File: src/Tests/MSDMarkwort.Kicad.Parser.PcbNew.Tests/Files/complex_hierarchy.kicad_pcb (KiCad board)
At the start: 2 copper layers, 100.7 x 80 mm, 68 parts, among them P101 CONN_2, P102 CONN_2, P201 CONN_2, P202 CONN_2, P301 CONN_2, P302 CONN_2, Q201 MPSA92, Q202 MPSA42, Q203 MPSA92, Q204 MPSA42, Q301 MPSA92, Q302 MPSA42, Q303 MPSA92, Q304 MPSA42, U101 78L05, U102 ICL7660, U201 LM358N, U301 LM358N

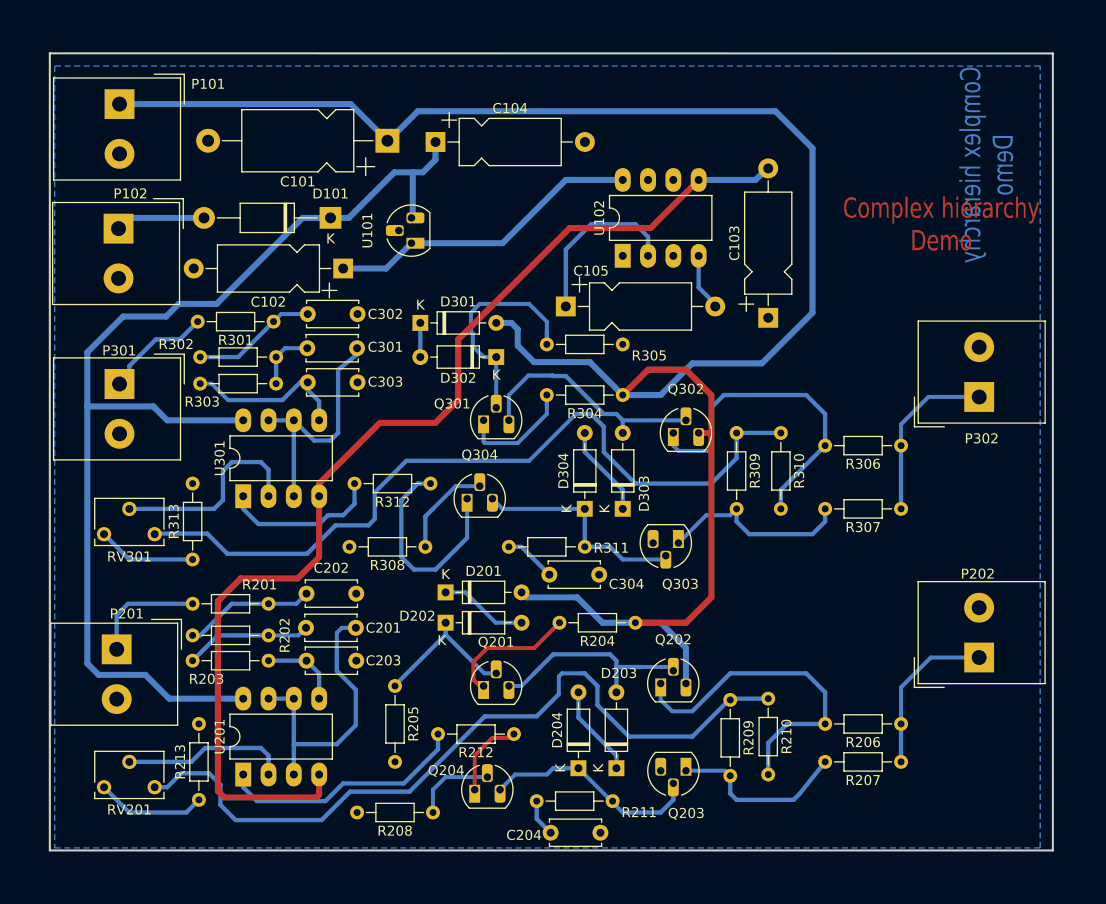
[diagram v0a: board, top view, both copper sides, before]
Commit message: eeschema parser added (#2)
* s-expression parser added
* eeschema parser  & models added
* readme changed
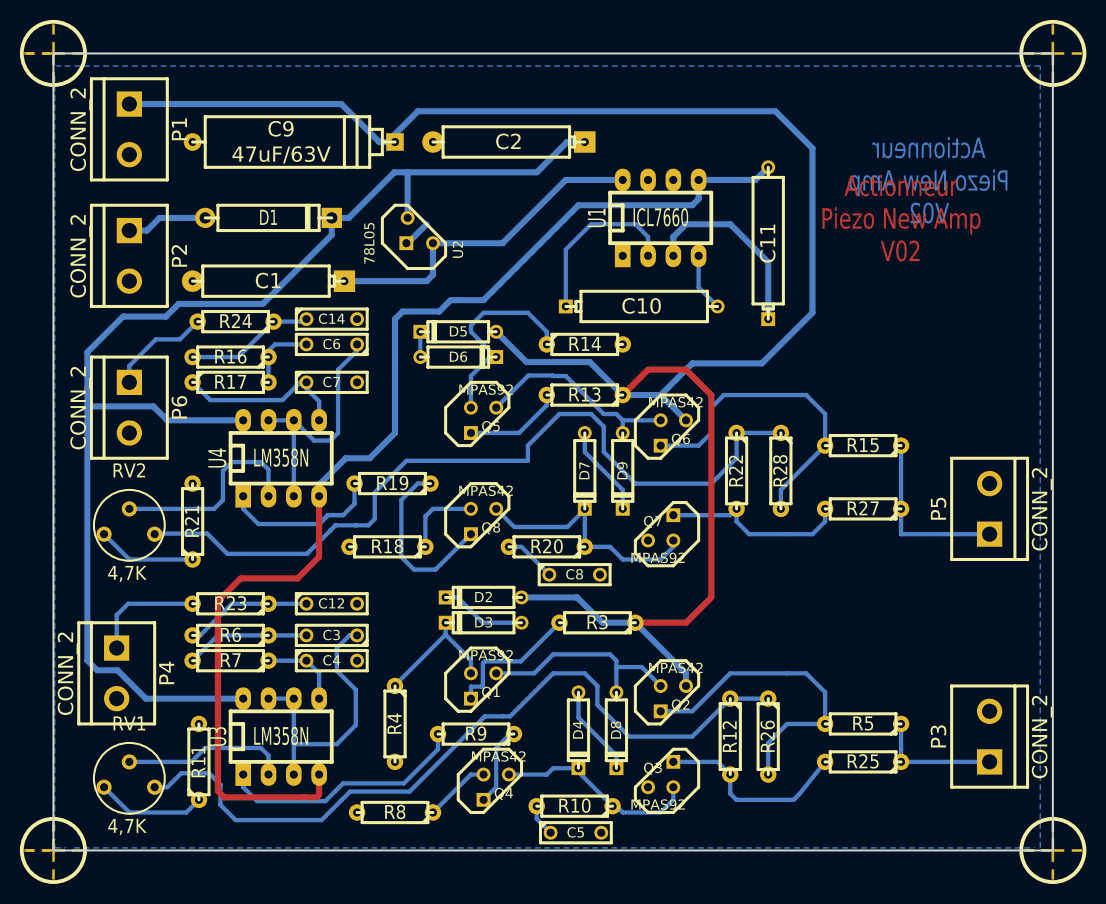
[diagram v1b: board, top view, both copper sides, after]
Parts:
- removed C101: 47uF/63V, Capacitor_THT:CP_Axial_L11.0mm_D6.0mm_P18.00mm_Horizontal
- removed C102: 47uF, Capacitor_THT:CP_Axial_L10.0mm_D4.5mm_P15.00mm_Horizontal
- removed C103, C105: 10uF, Capacitor_THT:CP_Axial_L10.0mm_D4.5mm_P15.00mm_Horizontal
- removed C104: 47uF/20V, Capacitor_THT:CP_Axial_L10.0mm_D4.5mm_P15.00mm_Horizontal
- removed C201, C301: 15nF, Capacitor_THT:C_Disc_D5.0mm_W2.5mm_P5.00mm
- removed C202, C302: 150nF, Capacitor_THT:C_Disc_D5.0mm_W2.5mm_P5.00mm
- removed C203, C303: 4.7nF, Capacitor_THT:C_Disc_D5.0mm_W2.5mm_P5.00mm
- removed C204, C304: 820pF, Capacitor_THT:C_Disc_D5.0mm_W2.5mm_P5.00mm
- removed D101: 1N4007, Diode_THT:D_DO-41_SOD81_P12.70mm_Horizontal
- removed D201, D202, D203, D204, D301, D302, D303, D304: 1N4148, Diode_THT:D_DO-35_SOD27_P7.62mm_Horizontal
- removed P101, P102, P201, P202, P301, P302: CONN_2, TerminalBlock_Altech:Altech_AK300_1x02_P5.00mm_45-Degree
- removed Q201, Q203, Q301, Q303: MPSA92, Package_TO_SOT_THT:TO-92_HandSolder
- removed Q202, Q204, Q302, Q304: MPSA42, Package_TO_SOT_THT:TO-92_HandSolder
- removed R201, R208, R212, R301, R308, R312: 1K, Resistor_THT:R_Axial_DIN0204_L3.6mm_D1.6mm_P7.62mm_Horizontal
- removed R202, R203, R302, R303: 22K, Resistor_THT:R_Axial_DIN0204_L3.6mm_D1.6mm_P7.62mm_Horizontal
- removed R204, R304: 470, Resistor_THT:R_Axial_DIN0204_L3.6mm_D1.6mm_P7.62mm_Horizontal
- removed R205, R209, R210, R305, R309, R310: 220K, Resistor_THT:R_Axial_DIN0204_L3.6mm_D1.6mm_P7.62mm_Horizontal
- removed R206, R207, R306, R307: 47, Resistor_THT:R_Axial_DIN0204_L3.6mm_D1.6mm_P7.62mm_Horizontal
- removed R211, R311: 5,6K, Resistor_THT:R_Axial_DIN0204_L3.6mm_D1.6mm_P7.62mm_Horizontal
- removed R213, R313: 4,7K, Resistor_THT:R_Axial_DIN0204_L3.6mm_D1.6mm_P7.62mm_Horizontal
- removed RV201, RV301: 4,7K, Potentiometer_THT:Potentiometer_Bourns_3266W_Vertical
- removed U101: 78L05, Package_TO_SOT_THT:TO-92_HandSolder
- removed U102: ICL7660, Package_DIP:DIP-8_W7.62mm_LongPads
- removed U201, U301: LM358N, Package_DIP:DIP-8_W7.62mm_LongPads
- added C1: 47uF, CP6, F.Cu at (109.9, 74.7)
- added C10: 10uF, CP6, F.Cu at (147.3, 77.2)
- added C11: 10uF, CP6, F.Cu at (160.0, 70.9)
- added C12: 150nF, C2, F.Cu at (116.2, 107.1)
- added C14: 150nF, C2, F.Cu at (116.2, 78.5)
- added C2: 47uF/20V, CP6, F.Cu at (134.0, 60.7)
- added C3: 15nF, C2, F.Cu at (116.2, 110.2)
- added C4: 4,7nF, C2, F.Cu at (116.2, 112.8)
- added C5: 820pF, C2, F.Cu at (140.7, 130.0)
- added C6: 15nF, C2, F.Cu at (116.2, 81.0)
- added C7: 4,7nF, C2, F.Cu at (116.2, 84.8)
- added C8: 820pF, C2, F.Cu at (140.6, 104.1)
- added C9: 47uF/63V, CP8, F.Cu at (112.4, 60.7)
- added D1: 1N4007, D5, F.Cu at (109.9, 68.3)
- added D2: 1N4148, D3, F.Cu at (131.4, 106.4)
- added D3: 1N4148, D3, F.Cu at (131.4, 109.0)
- added D4: 1N4148, D3, F.Cu at (141.0, 119.8)
- added D5: 1N4148, D3, F.Cu at (128.9, 79.8)
- added D6: 1N4148, D3, F.Cu at (128.9, 82.3)
- added D7: 1N4148, D3, F.Cu at (141.6, 93.7)
- added D8: 1N4148, D3, F.Cu at (144.8, 119.8)
- added D9: 1N4148, D3, F.Cu at (145.4, 93.7)
- added MIRE: *, MIRE, F.Cu at (188.6, 51.8)
- added MIRE: *, MIRE, F.Cu at (88.3, 51.8)
- added MIRE: *, MIRE, F.Cu at (88.3, 131.8)
- added MIRE: *, MIRE, F.Cu at (188.6, 131.8)
- added P1: CONN_2, bornier2, F.Cu at (95.9, 59.4)
- added P2: CONN_2, bornier2, F.Cu at (95.9, 72.1)
- added P3: CONN_2, bornier2, F.Cu at (182.2, 120.4)
- added P4: CONN_2, bornier2, F.Cu at (94.6, 114.0)
- added P5: CONN_2, bornier2, F.Cu at (182.2, 97.5)
- added P6: CONN_2, bornier2, F.Cu at (95.9, 87.4)
- added Q1: MPAS92, TO92-CBE, F.Cu at (131.4, 115.3)
- added Q2: MPAS42, TO92-CBE, F.Cu at (150.5, 116.6)
- added Q3: MPAS92, TO92-CBE, F.Cu at (149.2, 124.2)
- added Q4: MPAS42, TO92-CBE, F.Cu at (132.7, 125.5)
- added Q5: MPAS92, TO92-CBE, F.Cu at (131.4, 88.6)
- added Q6: MPAS42, TO92-CBE, F.Cu at (150.5, 89.9)
- added Q7: MPAS92, TO92-CBE, F.Cu at (149.2, 99.4)
- added Q8: MPAS42, TO92-CBE, F.Cu at (131.4, 98.8)
- added R10: 5,6K, R3-LARGE_PADS, F.Cu at (140.6, 127.4)
- added R11: 4,7K, R3-LARGE_PADS, F.Cu at (102.9, 122.9)
- added R12: 220K, R3-LARGE_PADS, F.Cu at (156.2, 120.4)
- added R13: 470, R3-LARGE_PADS, F.Cu at (141.6, 86.1)
- added R14: 220K, R3-LARGE_PADS, F.Cu at (141.6, 81.0)
- added R15: 47, R3-LARGE_PADS, F.Cu at (169.5, 91.2)
- added R16: 22K, R3-LARGE_PADS, F.Cu at (106.0, 82.3)
- added R17: 22K, R3-LARGE_PADS, F.Cu at (106.0, 84.8)
- added R18: 1K, R3-LARGE_PADS, F.Cu at (121.8, 101.3)
- added R19: 1K, R3-LARGE_PADS, F.Cu at (122.3, 95.0)
- added R20: 5,6K, R3-LARGE_PADS, F.Cu at (137.8, 101.3)
- added R21: 4,7K, R3-LARGE_PADS, F.Cu at (102.2, 98.8)
- added R22: 220K, R3-LARGE_PADS, F.Cu at (156.8, 93.7)
- added R23: 1K, R3-LARGE_PADS, F.Cu at (106.0, 107.1)
- added R24: 1K, R3-LARGE_PADS, F.Cu at (106.6, 78.7)
- added R25: 47, R3-LARGE_PADS, F.Cu at (169.5, 122.9)
- added R26: 220K, R3-LARGE_PADS, F.Cu at (160.0, 120.4)
- added R27: 47, R3-LARGE_PADS, F.Cu at (169.5, 97.5)
- added R28: 220K, R3-LARGE_PADS, F.Cu at (161.3, 93.7)
- added R3: 470, R3-LARGE_PADS, F.Cu at (142.9, 109.0)
- added R4: 220K, R3-LARGE_PADS, F.Cu at (122.6, 119.1)
- added R5: 47, R3-LARGE_PADS, F.Cu at (169.5, 119.1)
- added R6: 22K, R3-LARGE_PADS, F.Cu at (106.0, 110.2)
- added R7: 22K, R3-LARGE_PADS, F.Cu at (106.0, 112.8)
- added R8: 1K, R3-LARGE_PADS, F.Cu at (122.6, 128.0)
- added R9: 1K, R3-LARGE_PADS, F.Cu at (130.7, 120.1)
- added RV1: 4,7K, RV2, F.Cu at (95.9, 124.2)
- added RV2: 4,7K, RV2, F.Cu at (95.9, 98.8)
- added U1: ICL7660, DIP-8__300_ELL, F.Cu at (149.2, 68.3)
- added U2: 78L05, LM78LXX, F.Cu at (125.1, 69.6)
- added U3: LM358N, DIP-8__300_ELL, F.Cu at (111.1, 120.4)
- added U4: LM358N, DIP-8__300_ELL, F.Cu at (111.1, 92.5)
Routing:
- net /ampli_h8: track 0.00 -> 80.0 mm
- net /ampli_ht_horizontal/S_OUT+: track 79.2 -> 0.00 mm
- net /ampli_ht_vertical/S_OUT+: track 77.8 -> 0.00 mm
- net /ampli_h7: track 0.00 -> 76.7 mm
- net Net-(Q202-E): track 33.9 -> 0.00 mm
- net Net-(Q302-E): track 33.6 -> 0.00 mm
- net N-000037: track 0.00 -> 32.3 mm
- net N-000016: track 0.00 -> 31.7 mm
- net /ampli_ht_vertical/Vpil_0_3,3V: track 29.3 -> 0.00 mm
- net /ampli_h1: track 0.00 -> 28.3 mm
- net /ampli_h2: track 0.00 -> 25.4 mm
- net /ampli_ht_horizontal/Vpil_0_3,3V: track 25.2 -> 0.00 mm
- net Net-(R212-Pad2): track 25.1 -> 0.00 mm
- net N-000021: track 0.00 -> 25.1 mm
- net N-000046: track 0.00 -> 24.9 mm
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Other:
- board size 100.7 x 80 mm -> 100.3 x 80 mm
- rule pad_to_mask_clearance: 0 -> 0.254
- board text added: "Actionneur Piezo New Amp V02"
- board text removed: "Complex hierarchy Demo"
